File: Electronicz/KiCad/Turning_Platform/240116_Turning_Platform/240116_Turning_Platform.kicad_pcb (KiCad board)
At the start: 2 copper layers, 104.1 x 58.4 mm, 14 parts, among them J1 StepperMotor, J2 StepperDriverA, J3 StepperDriverB, J5 +12V, J6 GND, J7 Display, J8 RotaryEncoder

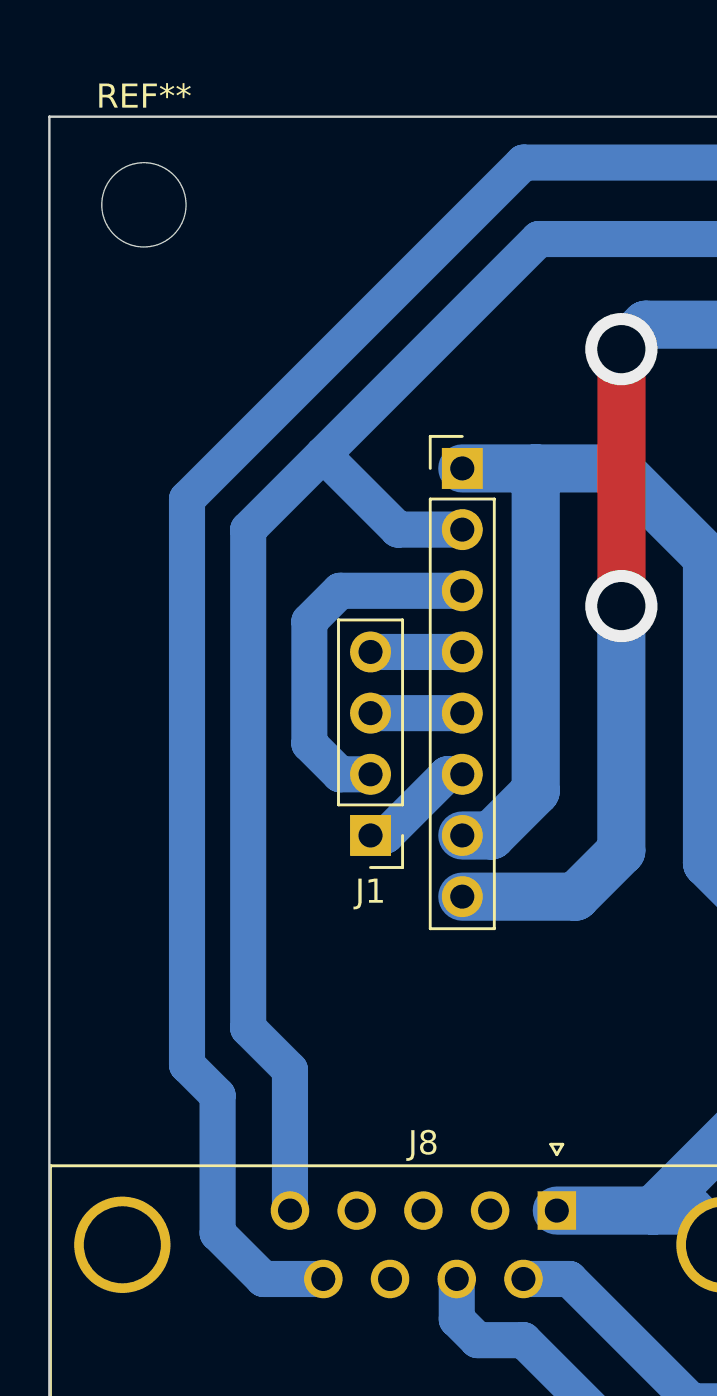
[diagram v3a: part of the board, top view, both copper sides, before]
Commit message: Update Stepper Connections Again because they are not the same on both StepperMotors
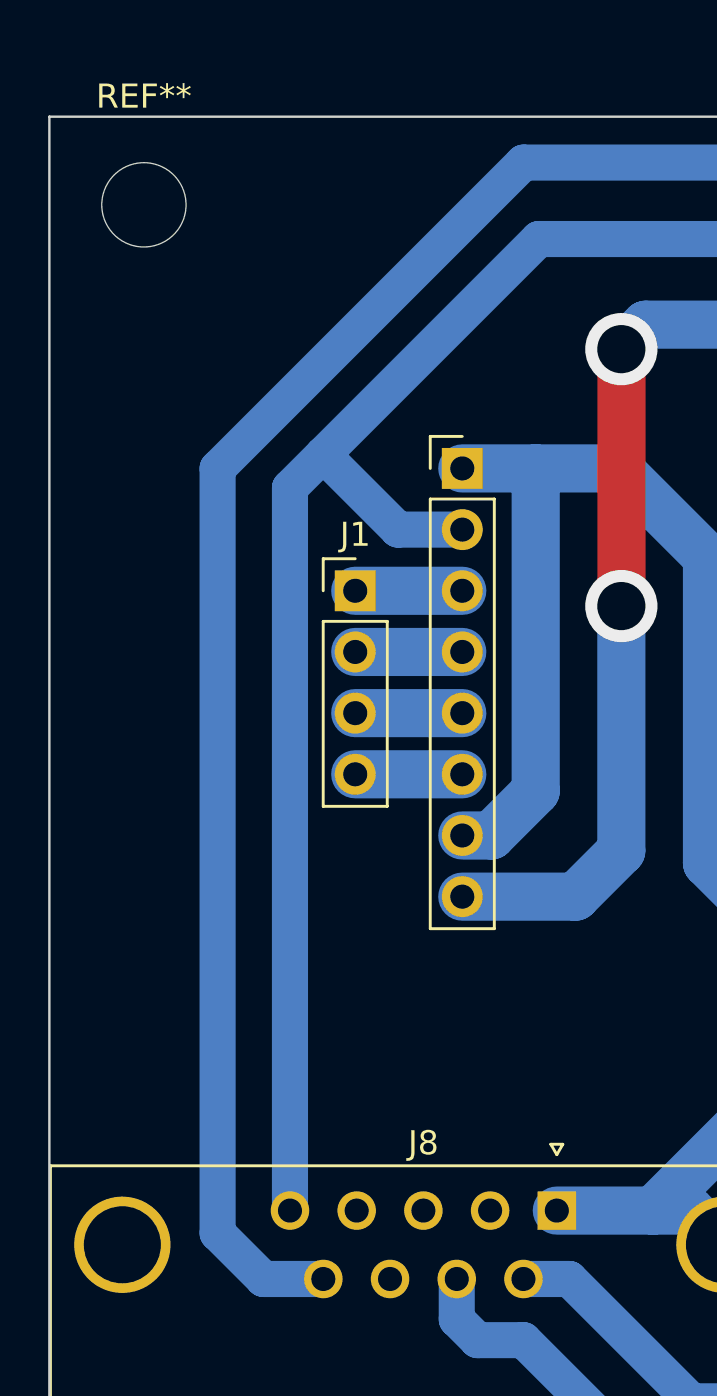
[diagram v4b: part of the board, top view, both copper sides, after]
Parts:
- moved J1 10.2 mm to (104.8, 73.0), turned to 0 degrees
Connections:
- J2 pad 3: Net-(J1-Pin_2) -> Net-(J1-Pin_1)
- J2 pad 4: Net-(J1-Pin_4) -> Net-(J1-Pin_2)
- J2 pad 6: Net-(J1-Pin_1) -> Net-(J1-Pin_4)
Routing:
- net Net-(J1-Pin_2): track 15.0 -> 4.44 mm
- net Net-(A1-+5V): track 196.3 -> 194.8 mm
- net Net-(A1-D4): track 144.3 -> 143.3 mm
- net Net-(J1-Pin_4): track 3.81 -> 4.44 mm
- net Net-(J1-Pin_3): track 3.81 -> 4.44 mm
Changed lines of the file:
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@@
   )
   (footprint "Connector_PinHeader_2.54mm:PinHeader_1x04_P2.54mm_Vertical" (layer "F.Cu")
-    (at 105.41 83.185 180)
+    (at 104.775 73.025)
     (descr "Through hole straight pin header, 1x04, 2.54mm pitch, single row")
     (tags "Through hole pin header THT 1x04 2.54mm single row")
@@
     (fp_line (start 1.27 8.89) (end -1.27 8.89)
       (stroke (width 0.1) (type solid)) (layer "F.Fab"))
-    (pad "1" thru_hole rect (at 0 0 180) (size 1.7 1.7) (drill 1) (layers "*.Cu" "*.Mask")
+    (pad "1" thru_hole rect (at 0 0) (size 1.7 1.7) (drill 1) (layers "*.Cu" "*.Mask")
       (net 27 "Net-(J1-Pin_1)") (pinfunction "Pin_1") (pintype "passive"))
-    (pad "2" thru_hole oval (at 0 2.54 180) (size 1.7 1.7) (drill 1) (layers "*.Cu" "*.Mask")
+    (pad "2" thru_hole oval (at 0 2.54) (size 1.7 1.7) (drill 1) (layers "*.Cu" "*.Mask")
       (net 28 "Net-(J1-Pin_2)") (pinfunction "Pin_2") (pintype "passive"))
-    (pad "3" thru_hole oval (at 0 5.08 180) (size 1.7 1.7) (drill 1) (layers "*.Cu" "*.Mask")
+    (pad "3" thru_hole oval (at 0 5.08) (size 1.7 1.7) (drill 1) (layers "*.Cu" "*.Mask")
       (net 29 "Net-(J1-Pin_3)") (pinfunction "Pin_3") (pintype "passive"))
-    (pad "4" thru_hole oval (at 0 7.62 180) (size 1.7 1.7) (drill 1) (layers "*.Cu" "*.Mask")
+    (pad "4" thru_hole oval (at 0 7.62) (size 1.7 1.7) (drill 1) (layers "*.Cu" "*.Mask")
       (net 30 "Net-(J1-Pin_4)") (pinfunction "Pin_4") (pintype "passive"))
     (model "${KICAD6_3DMODEL_DIR}/Connector_PinHeader_2.54mm.3dshapes/PinHeader_1x04_P2.54mm_Vertical.wrl"
@@
       (net 5 "Net-(A1-+5V)") (pinfunction "Pin_2") (pintype "passive"))
     (pad "3" thru_hole oval (at 0 5.08) (size 1.7 1.7) (drill 1) (layers "*.Cu" "*.Mask")
-      (net 28 "Net-(J1-Pin_2)") (pinfunction "Pin_3") (pintype "passive"))
+      (net 27 "Net-(J1-Pin_1)") (pinfunction "Pin_3") (pintype "passive"))
     (pad "4" thru_hole oval (at 0 7.62) (size 1.7 1.7) (drill 1) (layers "*.Cu" "*.Mask")
-      (net 30 "Net-(J1-Pin_4)") (pinfunction "Pin_4") (pintype "passive"))
+      (net 28 "Net-(J1-Pin_2)") (pinfunction "Pin_4") (pintype "passive"))
     (pad "5" thru_hole oval (at 0 10.16) (size 1.7 1.7) (drill 1) (layers "*.Cu" "*.Mask")
       (net 29 "Net-(J1-Pin_3)") (pinfunction "Pin_5") (pintype "passive"))
     (pad "6" thru_hole oval (at 0 12.7) (size 1.7 1.7) (drill 1) (layers "*.Cu" "*.Mask")
-      (net 27 "Net-(J1-Pin_1)") (pinfunction "Pin_6") (pintype "passive"))
+      (net 30 "Net-(J1-Pin_4)") (pinfunction "Pin_6") (pintype "passive"))
     (pad "7" thru_hole oval (at 0 15.24) (size 1.7 1.7) (drill 1) (layers "*.Cu" "*.Mask")
       (net 25 "Net-(J2-Pin_1)") (pinfunction "Pin_7") (pintype "passive"))
@@
   (via (at 151.765 65.405) (size 3) (drill 2) (layers "F.Cu" "B.Cu") (net 5))
   (via (at 151.765 58.42) (size 3) (drill 2) (layers "F.Cu" "B.Cu") (net 5))
-  (segment (start 100.33 70.485) (end 103.4415 67.3735) (width 1.5) (layer "B.Cu") (net 5))
-  (segment (start 100.33 91.186) (end 100.33 70.485) (width 1.5) (layer "B.Cu") (net 5))
   (segment (start 160.0835 85.7885) (end 163.195 88.9) (width 1.5) (layer "B.Cu") (net 5))
   (segment (start 183.605 94.445) (end 183.605 91.53) (width 1.5) (layer "B.Cu") (net 5))
   (segment (start 173.355 78.74) (end 175.26 78.74) (width 2) (layer "B.Cu") (net 5))
-  (segment (start 102.065 98.76) (end 102.065 92.921) (width 1.5) (layer "B.Cu") (net 5))
   (segment (start 151.765 64.77) (end 151.765 77.47) (width 1.5) (layer "B.Cu") (net 5))
   (segment (start 157.7975 83.5025) (end 160.0835 85.7885) (width 1.5) (layer "B.Cu") (net 5))
@@
   (segment (start 106.553 70.485) (end 103.4415 67.3735) (width 1.5) (layer "B.Cu") (net 5))
   (segment (start 163.195 88.9) (end 173.355 78.74) (width 2) (layer "B.Cu") (net 5))
+  (segment (start 102.065 98.76) (end 102.065 68.75) (width 1.5) (layer "B.Cu") (net 5))
   (segment (start 109.22 70.485) (end 106.553 70.485) (width 1.5) (layer "B.Cu") (net 5))
   (segment (start 142.748 97.536) (end 147.32 97.536) (width 1.5) (layer "B.Cu") (net 5))
   (segment (start 103.4415 67.3735) (end 112.395 58.42) (width 1.5) (layer "B.Cu") (net 5))
   (segment (start 182.245 90.17) (end 180.975 88.9) (width 1.5) (layer "B.Cu") (net 5))
-  (segment (start 102.065 92.921) (end 100.33 91.186) (width 1.5) (layer "B.Cu") (net 5))
   (segment (start 151.765 77.47) (end 157.7975 83.5025) (width 1.5) (layer "B.Cu") (net 5))
+  (segment (start 102.065 68.75) (end 103.4415 67.3735) (width 1.5) (layer "B.Cu") (net 5))
   (segment (start 112.395 58.42) (end 151.765 58.42) (width 1.5) (layer "B.Cu") (net 5))
   (segment (start 147.32 93.98) (end 157.7975 83.5025) (width 1.5) (layer "B.Cu") (net 5))
@@
   (via (at 146.685 65.405) (size 3) (drill 2) (layers "F.Cu" "B.Cu") (net 19))
   (via (at 146.685 55.245) (size 3) (drill 2) (layers "F.Cu" "B.Cu") (net 19))
-  (segment (start 99.06 99.695) (end 99.06 93.98) (width 1.5) (layer "B.Cu") (net 19))
-  (segment (start 99.06 93.98) (end 97.79 92.71) (width 1.5) (layer "B.Cu") (net 19))
-  (segment (start 97.79 69.215) (end 111.76 55.245) (width 1.5) (layer "B.Cu") (net 19))
+  (segment (start 99.06 67.945) (end 111.76 55.245) (width 1.5) (layer "B.Cu") (net 19))
+  (segment (start 100.965 101.6) (end 99.06 99.695) (width 1.5) (layer "B.Cu") (net 19))
+  (segment (start 103.45 101.6) (end 100.965 101.6) (width 1.5) (layer "B.Cu") (net 19))
   (segment (start 146.685 64.77) (end 146.685 84.455) (width 1.5) (layer "B.Cu") (net 19))
-  (segment (start 97.79 92.71) (end 97.79 69.215) (width 1.5) (layer "B.Cu") (net 19))
-  (segment (start 111.76 55.245) (end 146.685 55.245) (width 1.5) (layer "B.Cu") (net 19))
+  (segment (start 99.06 99.695) (end 99.06 67.945) (width 1.5) (layer "B.Cu") (net 19))
   (segment (start 139.192 91.948) (end 137.16 93.98) (width 1.5) (layer "B.Cu") (net 19))
   (segment (start 137.16 93.98) (end 127 93.98) (width 1.5) (layer "B.Cu") (net 19))
   (segment (start 146.685 84.455) (end 139.192 91.948) (width 1.5) (layer "B.Cu") (net 19))
-  (segment (start 103.45 101.6) (end 100.965 101.6) (width 1.5) (layer "B.Cu") (net 19))
-  (segment (start 100.965 101.6) (end 99.06 99.695) (width 1.5) (layer "B.Cu") (net 19))
+  (segment (start 111.76 55.245) (end 146.685 55.245) (width 1.5) (layer "B.Cu") (net 19))
   (segment (start 125.715 83.2) (end 127 81.915) (width 1.5) (layer "B.Cu") (net 20))
   (segment (start 127 81.915) (end 127 79.76) (width 1.5) (layer "B.Cu") (net 20))
@@
   (segment (start 121.92 85.74) (end 120.792 85.74) (width 2) (layer "B.Cu") (net 25))
   (segment (start 129.54 91.44) (end 124.46 91.44) (width 2) (layer "B.Cu") (net 25))
-  (segment (start 106.045 83.185) (end 108.585 80.645) (width 1.5) (layer "B.Cu") (net 27))
-  (segment (start 108.585 80.645) (end 109.22 80.645) (width 1.5) (layer "B.Cu") (net 27))
-  (segment (start 105.41 83.185) (end 106.045 83.185) (width 1.5) (layer "B.Cu") (net 27))
-  (segment (start 105.41 80.645) (end 104.14 80.645) (width 1.5) (layer "B.Cu") (net 28))
-  (segment (start 104.14 80.645) (end 102.87 79.375) (width 1.5) (layer "B.Cu") (net 28))
-  (segment (start 102.87 79.375) (end 102.87 74.295) (width 1.5) (layer "B.Cu") (net 28))
-  (segment (start 102.87 74.295) (end 104.14 73.025) (width 1.5) (layer "B.Cu") (net 28))
-  (segment (start 104.14 73.025) (end 109.22 73.025) (width 1.5) (layer "B.Cu") (net 28))
-  (segment (start 105.41 78.105) (end 109.22 78.105) (width 1.5) (layer "B.Cu") (net 29))
-  (segment (start 109.22 75.565) (end 105.41 75.565) (width 1.5) (layer "B.Cu") (net 30))
+  (segment (start 104.775 73.025) (end 109.22 73.025) (width 2) (layer "B.Cu") (net 27))
+  (segment (start 109.22 75.565) (end 104.775 75.565) (width 2) (layer "B.Cu") (net 28))
+  (segment (start 104.775 78.105) (end 109.22 78.105) (width 2) (layer "B.Cu") (net 29))
+  (segment (start 109.22 80.645) (end 104.775 80.645) (width 2) (layer "B.Cu") (net 30))
 )

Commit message: Plot Turning Platform PCB
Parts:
- added C1: C, Capacitor_THT:CP_Radial_D10.0mm_P7.50mm, F.Cu at (97.2, 90.8)
- added R4: 100, Resistor_THT:R_Axial_DIN0207_L6.3mm_D2.5mm_P10.16mm_Horizontal, F.Cu at (112.4, 94.0)
- moved R2 16.3 mm to (135.9, 109.2)
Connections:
- J8 pad 0: Net-(J2-Pin_1) -> unconnected-(J8-PAD-Pad0)
- J8 pad 3: unconnected-(J8-Pad3) -> Net-(C1-Pad2)
- J8 pad 7: Net-(A1-D3) -> Net-(C1-Pad2)
- R2 pad 2: Net-(A1-D3) -> Net-(C1-Pad2)
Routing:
- net Net-(C1-Pad2): track 0.00 -> 40.8 mm
- net Net-(A1-D3): track 47.7 -> 16.1 mm
- net Net-(A1-+5V): track 194.8 -> 205.1 mm
- net Net-(J2-Pin_1): track 111.9 -> 116.9 mm
- net Net-(A1-D4): track 143.3 -> 142.8 mm
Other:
- board text added: "Turning Platform 5AHME 2023/24 Patzelt"
